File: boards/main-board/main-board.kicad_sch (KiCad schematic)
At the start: 15 parts, among them J1 Screw_Terminal_01x02, J2 USB_C_Receptacle, J5 DNF, SW1 SW_Push, U1 W25Q128JVS, U2 RP2040, Y1 ABLS-12.000MHz-B4-T

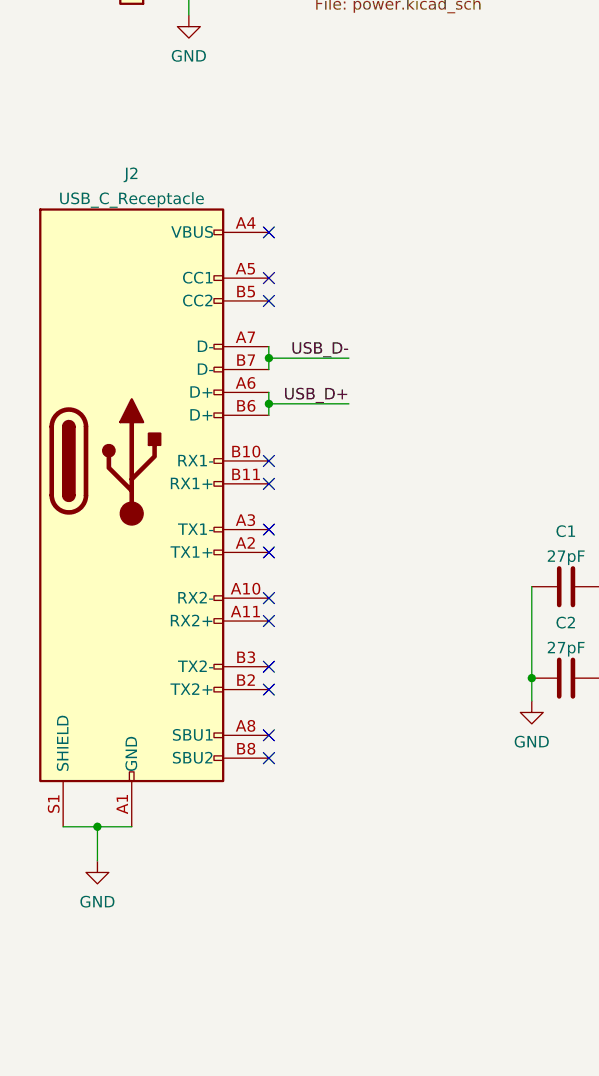
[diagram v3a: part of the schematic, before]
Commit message: Replaced USB C with micro usb
Signed-off-by: Computroniks <mnickson@sidingsmedia.com>
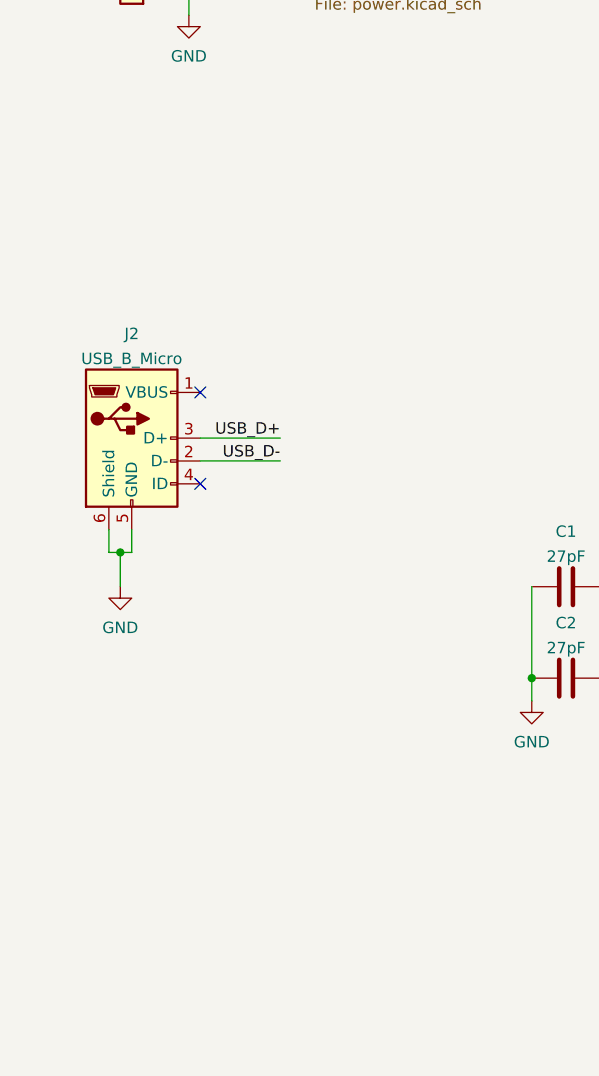
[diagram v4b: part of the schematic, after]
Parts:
- removed J2: USB_C_Receptacle, Connector_USB:USB_C_Receptacle_Amphenol_12401610E4-2A, symbol Connector:USB_C_Receptacle
- added J2: USB_B_Micro, Connector_USB:USB_Micro-B_Molex_47346-0001, symbol Connector:USB_B_Micro
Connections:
- net GND: now also J2.5 (GND), J2.6 (Shield)
- net USB_D+: now also J2.3 (D+)
- net USB_D-: now also J2.2 (D-)
- no-connect marks 35 -> 24
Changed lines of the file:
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@@
   (title_block
     (title "Main Board")
-    (date "2022-03-18")
-    (rev "V1.1.1")
+    (date "2022-03-19")
+    (rev "V1.1.2")
     (company "Matthew Nickson")
     (comment 1 "Licence: CC-BY-SA-4.0")
@@
   (junction (at 135.89 36.83) (diameter 0) (color 0 0 0 0)
   )
+  (junction (at 26.67 91.44) (diameter 0) (color 0 0 0 0)
+  )
   (junction (at 91.44 96.52) (diameter 0) (color 0 0 0 0)
   )
@@
   (junction (at 147.32 147.32) (diameter 0) (color 0 0 0 0)
   )
-  (junction (at 24.13 121.92) (diameter 0) (color 0 0 0 0)
-  )
-  (junction (at 43.18 69.85) (diameter 0) (color 0 0 0 0)
-  )
   (junction (at 149.86 36.83) (diameter 0) (color 0 0 0 0)
-  )
-  (junction (at 43.18 74.93) (diameter 0) (color 0 0 0 0)
   )
   (junction (at 152.4 36.83) (diameter 0) (color 0 0 0 0)
@@
   (no_connect (at 185.42 68.58))
   (no_connect (at 185.42 71.12))
-  (no_connect (at 43.18 55.88))
-  (no_connect (at 43.18 81.28))
-  (no_connect (at 43.18 63.5))
-  (no_connect (at 43.18 60.96))
-  (no_connect (at 43.18 106.68))
-  (no_connect (at 43.18 104.14))
-  (no_connect (at 43.18 111.76))
-  (no_connect (at 43.18 114.3))
-  (no_connect (at 43.18 99.06))
-  (no_connect (at 43.18 96.52))
-  (no_connect (at 43.18 91.44))
-  (no_connect (at 43.18 88.9))
-  (no_connect (at 43.18 83.82))
   (no_connect (at 185.42 81.28))
   (no_connect (at 185.42 78.74))
@@
   (no_connect (at 185.42 96.52))
   (no_connect (at 185.42 93.98))
+  (no_connect (at 35.56 73.66))
+  (no_connect (at 35.56 83.82))
   (wire (pts (xy 229.87 77.47) (xy 240.03 77.47))
     (stroke (width 0) (type default) (color 0 0 0 0))
@@
     (stroke (width 0) (type default) (color 0 0 0 0))
   )
-  (wire (pts (xy 43.18 69.85) (xy 52.07 69.85))
+  (wire (pts (xy 35.56 81.28) (xy 44.45 81.28))
     (stroke (width 0) (type default) (color 0 0 0 0))
   )
@@
     (stroke (width 0) (type default) (color 0 0 0 0))
   )
+  (wire (pts (xy 27.94 91.44) (xy 27.94 88.9))
+    (stroke (width 0) (type default) (color 0 0 0 0))
+  )
   (wire (pts (xy 85.09 27.94) (xy 82.55 27.94))
     (stroke (width 0) (type default) (color 0 0 0 0))
@@
     (stroke (width 0) (type default) (color 0 0 0 0))
   )
+  (wire (pts (xy 26.67 91.44) (xy 27.94 91.44))
+    (stroke (width 0) (type default) (color 0 0 0 0))
+  )
   (wire (pts (xy 166.37 36.83) (xy 166.37 45.72))
     (stroke (width 0) (type default) (color 0 0 0 0))
@@
     (stroke (width 0) (type default) (color 0 0 0 0))
   )
-  (wire (pts (xy 24.13 121.92) (xy 24.13 125.73))
+  (wire (pts (xy 26.67 91.44) (xy 26.67 95.25))
     (stroke (width 0) (type default) (color 0 0 0 0))
   )
@@
     (stroke (width 0) (type default) (color 0 0 0 0))
   )
-  (wire (pts (xy 24.13 121.92) (xy 27.94 121.92))
-    (stroke (width 0) (type default) (color 0 0 0 0))
-  )
   (wire (pts (xy 91.44 96.52) (xy 114.3 96.52))
     (stroke (width 0) (type default) (color 0 0 0 0))
@@
     (stroke (width 0) (type default) (color 0 0 0 0))
   )
-  (wire (pts (xy 43.18 68.58) (xy 43.18 69.85))
-    (stroke (width 0) (type default) (color 0 0 0 0))
-  )
-  (wire (pts (xy 43.18 73.66) (xy 43.18 74.93))
-    (stroke (width 0) (type default) (color 0 0 0 0))
-  )
   (wire (pts (xy 91.44 104.14) (xy 101.6 104.14))
     (stroke (width 0) (type default) (color 0 0 0 0))
@@
     (stroke (width 0) (type default) (color 0 0 0 0))
   )
+  (wire (pts (xy 25.4 91.44) (xy 26.67 91.44))
+    (stroke (width 0) (type default) (color 0 0 0 0))
+  )
   (wire (pts (xy 185.42 114.3) (xy 198.12 114.3))
     (stroke (width 0) (type default) (color 0 0 0 0))
@@
     (stroke (width 0) (type default) (color 0 0 0 0))
   )
-  (wire (pts (xy 43.18 69.85) (xy 43.18 71.12))
-    (stroke (width 0) (type default) (color 0 0 0 0))
-  )
   (wire (pts (xy 80.01 96.52) (xy 91.44 96.52))
     (stroke (width 0) (type default) (color 0 0 0 0))
@@
     (stroke (width 0) (type default) (color 0 0 0 0))
   )
-  (wire (pts (xy 43.18 74.93) (xy 43.18 76.2))
-    (stroke (width 0) (type default) (color 0 0 0 0))
-  )
   (wire (pts (xy 82.55 27.94) (xy 82.55 30.48))
     (stroke (width 0) (type default) (color 0 0 0 0))
   )
-  (wire (pts (xy 20.32 121.92) (xy 24.13 121.92))
-    (stroke (width 0) (type default) (color 0 0 0 0))
-  )
   (wire (pts (xy 80.01 95.25) (xy 80.01 96.52))
     (stroke (width 0) (type default) (color 0 0 0 0))
@@
     (stroke (width 0) (type default) (color 0 0 0 0))
   )
+  (wire (pts (xy 25.4 88.9) (xy 25.4 91.44))
+    (stroke (width 0) (type default) (color 0 0 0 0))
+  )
   (wire (pts (xy 97.79 116.84) (xy 101.6 116.84))
     (stroke (width 0) (type default) (color 0 0 0 0))
   )
-  (wire (pts (xy 43.18 74.93) (xy 52.07 74.93))
+  (wire (pts (xy 35.56 78.74) (xy 44.45 78.74))
     (stroke (width 0) (type default) (color 0 0 0 0))
   )
@@
     (effects (font (size 1.27 1.27)) (justify right bottom))
   )
-  (label "USB_D+" (at 52.07 74.93 180)
+  (label "USB_D+" (at 44.45 78.74 180)
     (effects (font (size 1.27 1.27)) (justify right bottom))
   )
@@
     (effects (font (size 1.27 1.27)) (justify left bottom))
   )
-  (label "USB_D-" (at 52.07 69.85 180)
+  (label "USB_D-" (at 44.45 81.28 180)
     (effects (font (size 1.27 1.27)) (justify right bottom))
   )
@@
     (pin "9")
   )
+  (symbol (lib_id "Connector:USB_B_Micro") (at 27.94 78.74 0) (unit 1)
+    (in_bom yes) (on_board yes) (fields_autoplaced)
+    (property "Reference" "J2" (id 0) (at 27.94 67.1535 0))
+    (property "Value" "USB_B_Micro" (id 1) (at 27.94 69.9286 0))
+    (property "Footprint" "Connector_USB:USB_Micro-B_Molex_47346-0001" (id 2) (at 31.75 80.01 0)
+      (effects (font (size 1.27 1.27)) hide)
+    )
+    (property "Datasheet" "~" (id 3) (at 31.75 80.01 0)
+      (effects (font (size 1.27 1.27)) hide)
+    )
+    (pin "1")
+    (pin "2")
+    (pin "3")
+    (pin "4")
+    (pin "5")
+    (pin "6")
+  )
   (symbol (lib_id "power:GND") (at 82.55 30.48 0) (unit 1)
     (in_bom yes) (on_board yes) (fields_autoplaced)
@@
     (pin "2")
   )
-  (symbol (lib_id "power:GND") (at 24.13 125.73 0) (unit 1)
-    (in_bom yes) (on_board yes) (fields_autoplaced)
-    (property "Reference" "#PWR021" (id 0) (at 24.13 132.08 0)
-      (effects (font (size 1.27 1.27)) hide)
-    )
-    (property "Value" "GND" (id 1) (at 24.13 130.2925 0))
-    (property "Footprint" "" (id 2) (at 24.13 125.73 0)
-      (effects (font (size 1.27 1.27)) hide)
-    )
-    (property "Datasheet" "" (id 3) (at 24.13 125.73 0)
+  (symbol (lib_id "power:GND") (at 26.67 95.25 0) (unit 1)
+    (in_bom yes) (on_board yes) (fields_autoplaced)
+    (property "Reference" "#PWR021" (id 0) (at 26.67 101.6 0)
+      (effects (font (size 1.27 1.27)) hide)
+    )
+    (property "Value" "GND" (id 1) (at 26.67 99.8125 0))
+    (property "Footprint" "" (id 2) (at 26.67 95.25 0)
+      (effects (font (size 1.27 1.27)) hide)
+    )
+    (property "Datasheet" "" (id 3) (at 26.67 95.25 0)
       (effects (font (size 1.27 1.27)) hide)
     )
@@
     (pin "1")
   )
-  (symbol (lib_id "Connector:USB_C_Receptacle") (at 27.94 81.28 0) (unit 1)
-    (in_bom yes) (on_board yes)
-    (property "Reference" "J2" (id 0) (at 27.94 49.3735 0))
-    (property "Value" "USB_C_Receptacle" (id 1) (at 27.94 52.1486 0))
-    (property "Footprint" "Connector_USB:USB_C_Receptacle_Amphenol_12401610E4-2A" (id 2) (at 31.75 81.28 0)
-      (effects (font (size 1.27 1.27)) hide)
-    )
-    (property "Datasheet" "https://www.usb.org/sites/default/files/documents/usb_type-c.zip" (id 3) (at 31.75 81.28 0)
-      (effects (font (size 1.27 1.27)) hide)
-    )
-    (pin "A1")
-    (pin "A10")
-    (pin "A11")
-    (pin "A12")
-    (pin "A2")
-    (pin "A3")
-    (pin "A4")
-    (pin "A5")
-    (pin "A6")
-    (pin "A7")
-    (pin "A8")
-    (pin "A9")
-    (pin "B1")
-    (pin "B10")
-    (pin "B11")
-    (pin "B12")
-    (pin "B2")
-    (pin "B3")
-    (pin "B4")
-    (pin "B5")
-    (pin "B6")
-    (pin "B7")
-    (pin "B8")
-    (pin "B9")
-    (pin "S1")
-  )
   (sheet (at 48.26 24.13) (size 12.7 5.08) (fields_autoplaced)
     (stroke (width 0.1524) (type solid) (color 0 0 0 0))
@@
       (reference "J1") (unit 1) (value "Screw_Terminal_01x02") (footprint "TerminalBlock:TerminalBlock_Altech_AK300-2_P5.00mm")
     )
-    (path "/f1f41418-7707-4d69-9dd5-cce92de8cb12"
-      (reference "J2") (unit 1) (value "USB_C_Receptacle") (footprint "Connector_USB:USB_C_Receptacle_Amphenol_12401610E4-2A")
+    (path "/22becf65-b34a-4371-9033-b7ccd8d61645"
+      (reference "J2") (unit 1) (value "USB_B_Micro") (footprint "Connector_USB:USB_Micro-B_Molex_47346-0001")
     )
     (path "/29939343-0bb1-4b43-b3b0-44cc3beab70b/6749e8ed-a97b-4ff2-8030-b0426ecba43c"

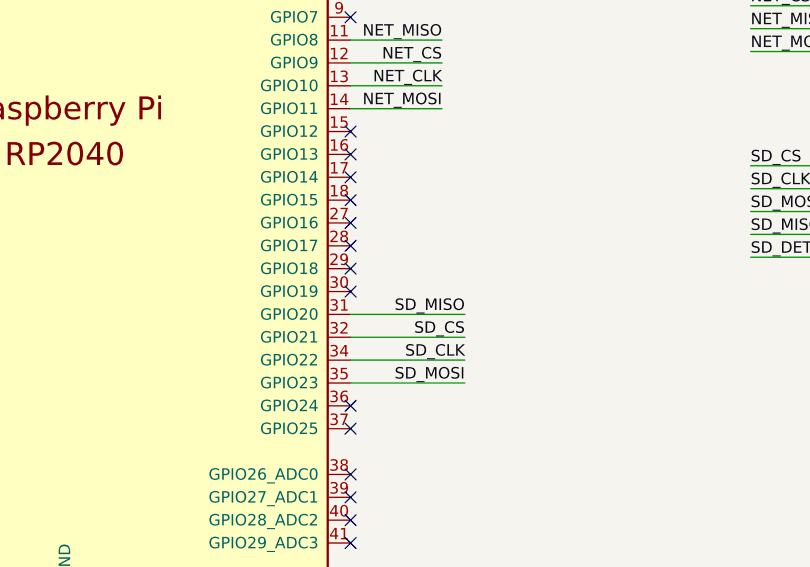
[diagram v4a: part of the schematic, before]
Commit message: Added SD_DET to RP2040
Signed-off-by: Computroniks <mnickson@sidingsmedia.com>
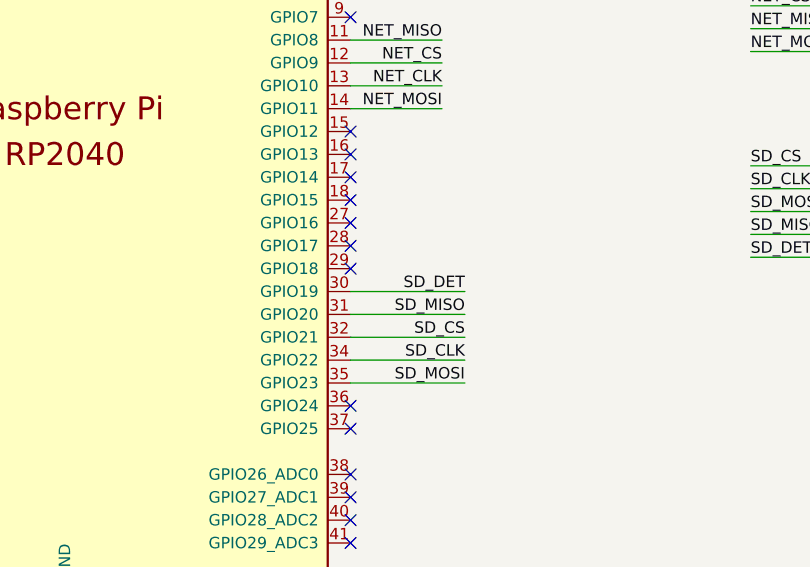
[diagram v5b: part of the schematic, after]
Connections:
- net SD_DET: now also U2.30 (GPIO19)
- no-connect marks 24 -> 23
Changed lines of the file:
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@@
   (no_connect (at 185.42 127))
   (no_connect (at 185.42 124.46))
-  (no_connect (at 185.42 111.76))
   (no_connect (at 185.42 63.5))
   (no_connect (at 185.42 66.04))
@@
     (stroke (width 0) (type default) (color 0 0 0 0))
   )
+  (wire (pts (xy 185.42 111.76) (xy 198.12 111.76))
+    (stroke (width 0) (type default) (color 0 0 0 0))
+  )
   (wire (pts (xy 229.87 107.95) (xy 240.03 107.95))
     (stroke (width 0) (type default) (color 0 0 0 0))
@@
     (effects (font (size 1.27 1.27)) (justify left bottom))
   )
+  (label "SD_DET" (at 198.12 111.76 180)
+    (effects (font (size 1.27 1.27)) (justify right bottom))
+  )
   (label "SD_MISO" (at 198.12 114.3 180)
